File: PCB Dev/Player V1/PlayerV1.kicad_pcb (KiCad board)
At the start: 2 copper layers, 24 parts, among them U1 AP7217A, U2 AK4619VN, U3 ESP32-S3-WROOM-1-N8R8

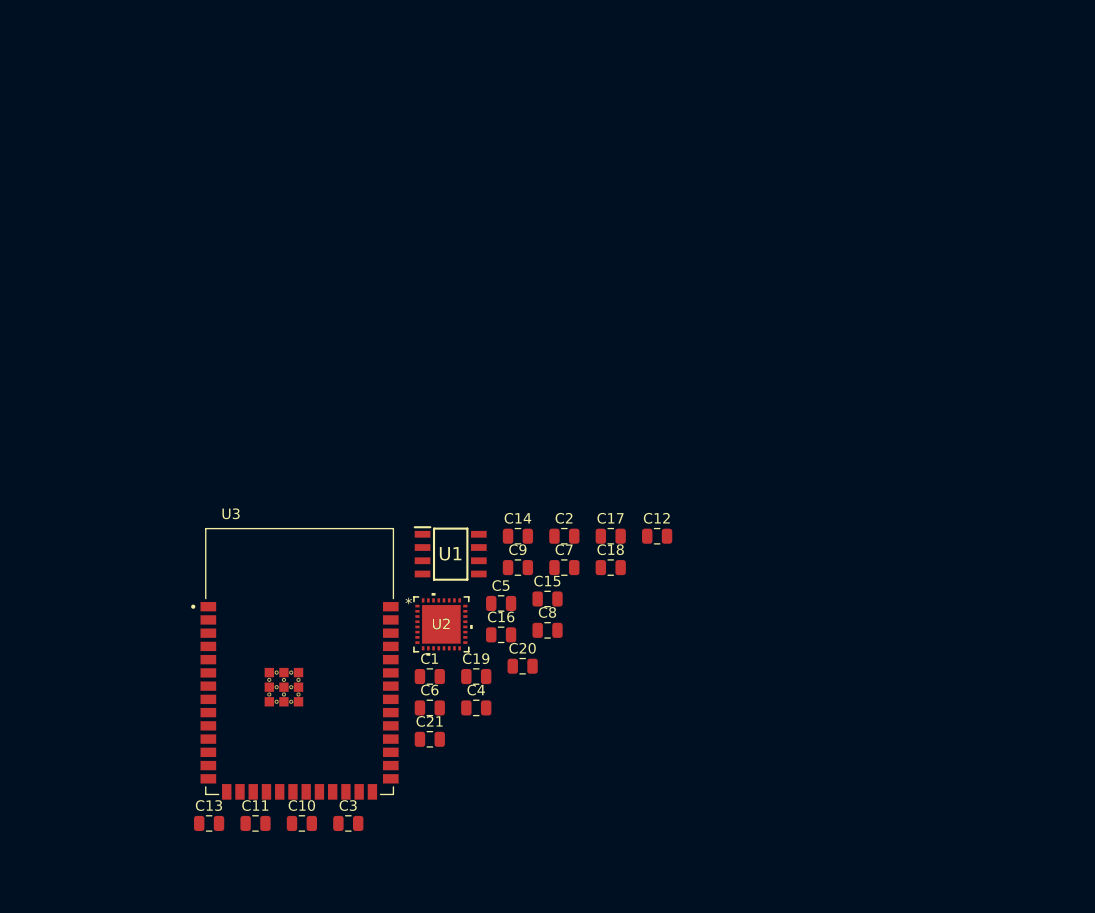
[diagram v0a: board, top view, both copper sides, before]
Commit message: PCB Dev
Added headphone jacks amp, and stereo speakers amp

added gui interface buttons though they may have to be put in another pcb

learned esp32 s3 does not have bluetooth a2dp so I need to switch to esp32 wroom 32E with 16mb instead only issue is gpio are becoming scarce
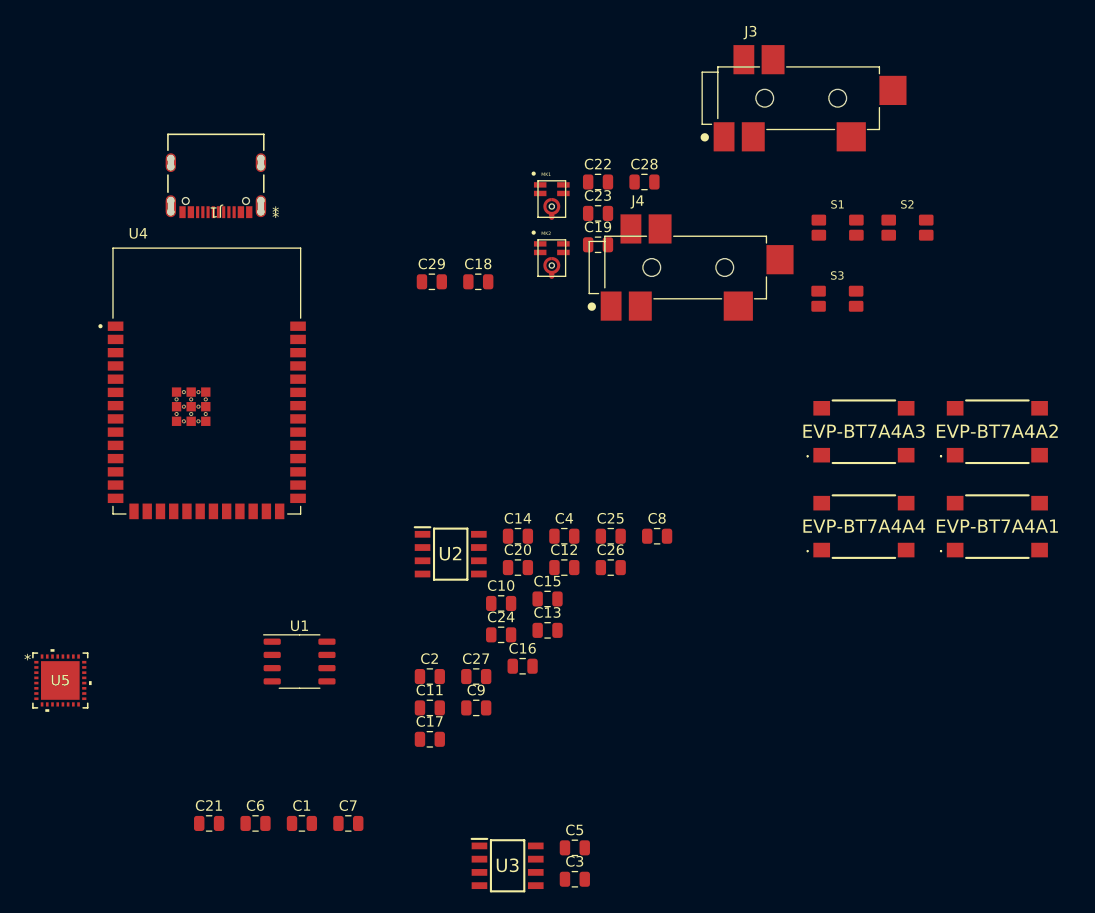
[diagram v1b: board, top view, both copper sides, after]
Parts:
- added C18: 1uF, Capacitor_SMD:C_0805_2012Metric, F.Cu at (137.3, 58.9)
- added C19: 1uF, Capacitor_SMD:C_0805_2012Metric, F.Cu at (148.8, 55.3)
- added C22: 0.1uF, Capacitor_SMD:C_0805_2012Metric, F.Cu at (148.8, 49.3)
- added C23: 0.1uF, Capacitor_SMD:C_0805_2012Metric, F.Cu at (148.8, 52.3)
- added C28: 10uF, Capacitor_SMD:C_0805_2012Metric, F.Cu at (153.3, 49.3)
- added C29: 10uF, Capacitor_SMD:C_0805_2012Metric, F.Cu at (132.9, 58.9)
- added C3: 1uF, Capacitor_SMD:C_0805_2012Metric, F.Cu at (146.6, 116.2)
- added C5: 1uF, Capacitor_SMD:C_0805_2012Metric, F.Cu at (146.6, 113.2)
- added EVP-BT7A4A1: EVP-BT7A4A000, EVP-BT7A4A000:EVPBT7A4A000, F.Cu at (187.1, 82.3)
- added EVP-BT7A4A2: EVP-BT7A4A000, EVP-BT7A4A000:EVPBT7A4A000, F.Cu at (187.1, 73.2)
- added EVP-BT7A4A3: EVP-BT7A4A000, EVP-BT7A4A000:EVPBT7A4A000, F.Cu at (174.3, 73.2)
- added EVP-BT7A4A4: EVP-BT7A4A000, EVP-BT7A4A000:EVPBT7A4A000, F.Cu at (174.3, 82.3)
- added J1: USB_C_Receptacle_USB2.0, 12402012E212A:12402012E212A_AMP, F.Cu at (112.2, 48.5)
- added J3: SJ-43516-SMT-U, SJ-43516-SMT-GR:CUI_SJ-43516-SMT-GR, F.Cu at (168.0, 41.3)
- added J4: SJ-43516-SMT-U, SJ-43516-SMT-GR:CUI_SJ-43516-SMT-GR, F.Cu at (157.2, 57.5)
- added MK1: ICS-40618, ICS-40618:MIC_ICS-40618, F.Cu at (144.4, 50.9)
- added MK2: ICS-40618, ICS-40618:MIC_ICS-40618, F.Cu at (144.4, 56.6)
- added S1: EVQ-P7B01P, EVQ-P7B01P:EVQ-P7B01P, F.Cu at (171.8, 53.7)
- added S2: EVQ-P7B01P, EVQ-P7B01P:EVQ-P7B01P, F.Cu at (178.5, 53.7)
- added S3: EVQ-P7B01P, EVQ-P7B01P:EVQ-P7B01P, F.Cu at (171.8, 60.5)
- added U3: AP7217A, AP7217A:SOIC127P600X175-8N, F.Cu at (140.1, 114.9)
- added U4: ESP32-S3-WROOM-1-N8, ESP32-S3 Module:XCVR_ESP32S3WROOM1N8R8, F.Cu at (111.3, 68.4)
- C1: renamed from C10; value 0.1uF -> 10uF
- C14: value 10uF -> 0.1uF
- C15: value 10uF -> 1uF
- C16: renamed from C20; value 0.1uF -> 1uF
- C17: renamed from C21; value 0.1uF -> 1uF
- C6: renamed from C11; value 2.2uF -> 10uF
- C8: renamed from C12; value 0.1uF -> 2.2uF
- U1: renamed from U3; value ESP32-S3-WROOM-1-N8R8 -> TP4056; footprint ESP32-S3 Module:XCVR_ESP32S3WROOM1N8R8 -> Package_SO:SOP-8_3.9x4.9mm_P1.27mm
- moved U5 36.9 mm to (97.2, 97.1)
- renumbered C5 to C10, C6 to C11, C7 to C12, C8 to C13, C1 to C2, C9 to C20, C13 to C21, C16 to C24, C17 to C25, C18 to C26, C19 to C27, C2 to C4, C3 to C7, C4 to C9, U1 to U2, U2 to U5
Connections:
- C1 pad 2: Net-(C10-Pad2) -> Net-(C1-Pad2)
- C10 pad 1: unconnected-(C5-Pad1) -> /IN3N
- C10 pad 2: unconnected-(C5-Pad2) -> Net-(C10-Pad2)
- C11 pad 1: unconnected-(C6-Pad1) -> /IN4P
- C11 pad 2: unconnected-(C6-Pad2) -> Net-(C11-Pad2)
- C12 pad 1: unconnected-(C7-Pad1) -> /IN4N
- C12 pad 2: unconnected-(C7-Pad2) -> Net-(C12-Pad2)
- C13 pad 1: GNDREF -> GND
- C14 pad 1: Net-(C14-Pad1) -> GND
- C15 pad 1: Net-(C15-Pad1) -> /IN2N
- C16 pad 1: GND -> /IN2P
- C16 pad 2: Net-(C14-Pad1) -> unconnected-(C16-Pad2)
- C17 pad 1: GND -> /IN1N
- C17 pad 2: Net-(C15-Pad1) -> GND
- C2 pad 2: VCC -> GND
- C20 pad 1: GNDREF -> GND
- C24 pad 1: unconnected-(C16-Pad1) -> /AOUT2R
- C24 pad 2: unconnected-(C16-Pad2) -> Net-(C24-Pad2)
- C25 pad 1: unconnected-(C17-Pad1) -> /AOUT2L
- C25 pad 2: unconnected-(C17-Pad2) -> Net-(C25-Pad2)
- C26 pad 1: unconnected-(C18-Pad1) -> /AOUT1R
- C26 pad 2: unconnected-(C18-Pad2) -> Net-(C26-Pad2)
- C27 pad 1: unconnected-(C19-Pad1) -> /AOUT1L
- C27 pad 2: unconnected-(C19-Pad2) -> Net-(C27-Pad2)
- C6 pad 2: VCC -> +BATT
- C7 pad 2: GNDREF -> GND
- C8 pad 2: VCC -> GND
- C9 pad 1: unconnected-(C4-Pad1) -> /IN3P
- C9 pad 2: unconnected-(C4-Pad2) -> Net-(C9-Pad2)
- U1 pad 1: GND -> unconnected-(U1-Pad1)
- U1 pad 2: VCC -> Net-(R4-Pad2)
- U1 pad 3: Net-(C10-Pad2) -> GND
- U1 pad 4: unconnected-(U3-Pad4) -> Net-(C1-Pad2)
- U1 pad 5: unconnected-(U3-Pad5) -> +BATT
- U1 pad 6: unconnected-(U3-Pad6) -> Net-(R1-Pad2)
- U1 pad 7: unconnected-(U3-Pad7) -> Net-(R3-Pad2)
- U1 pad 8: unconnected-(U3-Pad8) -> Net-(C1-Pad2)
- U2 pad 2: VCC -> GND
- U5 pad 19: /VSS1 -> GND
- U5 pad 2: /SDIN2 -> GND
- U5 pad 20: /VREFL -> GND
- U5 pad 21: /VREFH -> GND
- U5 pad 4: GNDREF -> GND
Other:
- board outline added: 8.6 x 5.1 mm
